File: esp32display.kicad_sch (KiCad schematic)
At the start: 20 parts, among them J1 V_IN, J2 V_PANEL, J3 USB-C Power Only, J4 LIS3DH, J5 RGB_PANEL, J6 TOUCH, J7 NPX1, J8 NPX2, SW1 SW_Push, U1 AMS1117-3.3

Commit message: Started to change project in preparation for next version
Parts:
- removed D2, D3: WS2812B, LED_SMD:LED_WS2812B_PLCC4_5.0x5.0mm_P3.2mm, symbol LED:WS2812B
- removed J3: USB-C Power Only, usb-c_recepticle_LCSC-C165948_hand_solder:USB-C_LCSC_C165948_Hand_Solder, symbol Connector:USB_C_Receptacle_USB2.0
- removed J8: NPX2, Connector_PinHeader_2.54mm:PinHeader_1x03_P2.54mm_Vertical, symbol Connector_Generic:Conn_01x03
- removed R5: 10k, Resistor_SMD:R_0603_1608Metric_Pad0.98x0.95mm_HandSolder, symbol Device:R
- removed SW1: SW_Push, Button_Switch_SMD:SW_Push_1P1T_NO_CK_KSC7xxJ, symbol Switch:SW_Push
- added J3: USB_C_Receptacle_PowerOnly_6P, symbol Connector:USB_C_Receptacle_PowerOnly_6P
- added U3: LIS3DH, Package_LGA:LGA-16_3x3mm_P0.5mm_LayoutBorder3x5y, symbol Sensor_Motion:LIS3DH
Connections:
- net GND: now also J3.A12 (GND), J3.B12 (GND), J3.S1 (SHIELD)
- net NPX1: now also J7.2 (Pin_2)
- net at D1.2 (A): now also J3.A9 (VBUS), J3.B9 (VBUS)
- net at R1.1: now also J3.B5 (CC2)
- net at R2.1: now also J3.A5 (CC1)
- new net: U3.10 (GND), U3.12 (GND), U3.5 (GND)
- no-connect marks 7 -> 1
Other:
- moved on the sheet: D1

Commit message: Submitted V0.2 to production
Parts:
- removed J1: V_IN, Power_Pads:2 x 0.2 Pads, symbol Connector_Generic:Conn_01x02
- removed J4: LIS3DH, Connector_PinHeader_2.54mm:PinHeader_1x06_P2.54mm_Vertical, symbol Connector_Generic:Conn_01x06
- removed U1: AMS1117-3.3, Package_TO_SOT_SMD:SOT-223-3_TabPin2, symbol Regulator_Linear:AMS1117-3.3
- added U1: LD1117S12TR_SOT223, Package_TO_SOT_SMD:SOT-223-3_TabPin2, symbol Regulator_Linear:LD1117S12TR_SOT223
- J2: footprint Power_Pads:2 x 0.2 Pads -> Connector_PinHeader_2.54mm:PinHeader_1x02_P2.54mm_Vertical
- J3: footprint (none) -> Connector_USB:USB_C_Receptacle_GCT_USB4125-xx-x_6P_TopMnt_Horizontal; LCSC (none) -> C2689837
- J5: renamed from J6; footprint Connector_PinHeader_2.54mm:PinHeader_1x02_P2.54mm_Vertical -> Connector_JST:JST_PH_S2B-PH-K_1x02_P2.00mm_Horizontal
- J6: renamed from J7; footprint Connector_PinHeader_2.54mm:PinHeader_1x03_P2.54mm_Vertical -> Connector_JST:JST_PH_S3B-PH-K_1x03_P2.00mm_Horizontal
- R4: footprint OptoDevice:R_LDR_5.1x4.3mm_P3.4mm_Vertical -> Connector_JST:JST_PH_S2B-PH-K_1x02_P2.00mm_Horizontal
- renumbered J5 to J4, U3 to U2
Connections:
- net +3V3: now also U2.1 (VDD_IO), U2.14 (VDD), U2.8 (CS), U1.2 (VO)
- net +5V: now also U1.3 (VI); no longer J2.2 (Pin_2), J6.1 (Pin_1)
- net GND: now also U2.10 (GND), U2.12 (GND), U2.5 (GND), U1.1 (GND)
- net SCL: now also U2.4 (SPC)
- net SDA: now also U2.6 (SDI)
- net VBUS: now reaches D1.2 (A), J3.A9 (VBUS), J3.B9 (VBUS)
- net VBUS: now also J2.2 (Pin_2), J6.1 (Pin_1)
- net INT1: now reaches U2.11 (INT1)
- net INT2: now reaches U2.9 (INT2)
- no-connect marks 1 -> 4

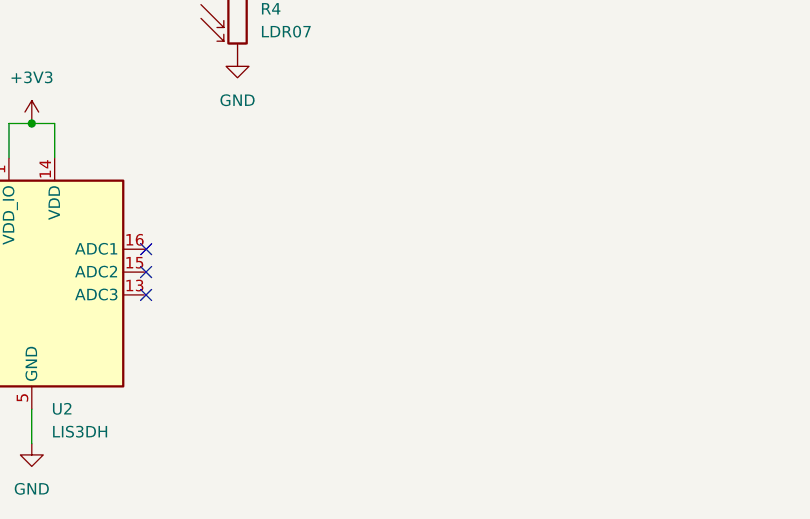
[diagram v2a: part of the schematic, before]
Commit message: Added I2C Pullup Resistors
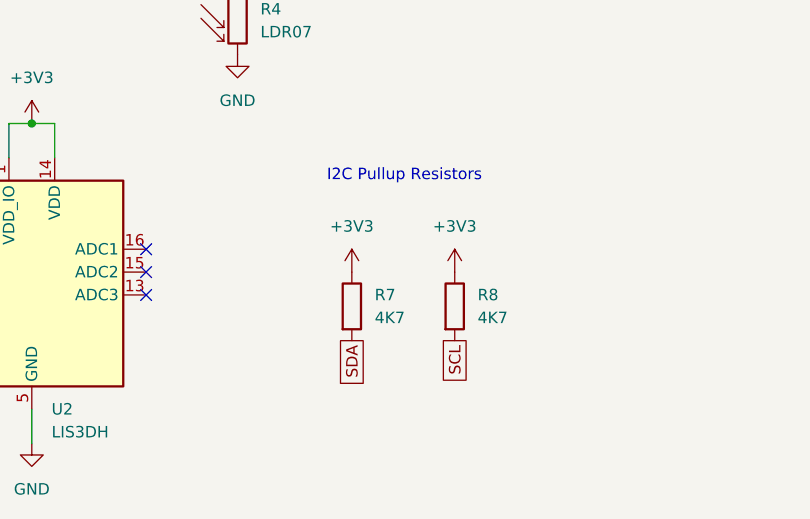
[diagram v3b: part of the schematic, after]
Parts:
- added R7, R8: 4K7, Resistor_SMD:R_0603_1608Metric_Pad0.98x0.95mm_HandSolder, symbol Device:R
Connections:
- net +3V3: now also R7.1, R8.1
- net SCL: now also R8.2
- net SDA: now also R7.2
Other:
- note added: "I2C Pullup Resistors"

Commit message: Minor fixes from V0.2.  Corrected C1 & C2 package sizes.  Improved pushbutton marking on silkscreen.
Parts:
- C1, C2: footprint Capacitor_SMD:C_1206_3216Metric -> Capacitor_SMD:C_0805_2012Metric
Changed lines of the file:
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@@
 			)
 		)
-		(property "Footprint" "Capacitor_SMD:C_1206_3216Metric"
+		(property "Footprint" "Capacitor_SMD:C_0805_2012Metric"
 			(at 96.2152 41.91 0)
 			(effects
@@
 			)
 		)
-		(property "Footprint" "Capacitor_SMD:C_1206_3216Metric"
+		(property "Footprint" "Capacitor_SMD:C_0805_2012Metric"
 			(at 75.8952 41.91 0)
 			(effects
